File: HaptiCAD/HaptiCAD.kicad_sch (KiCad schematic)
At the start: 0 parts

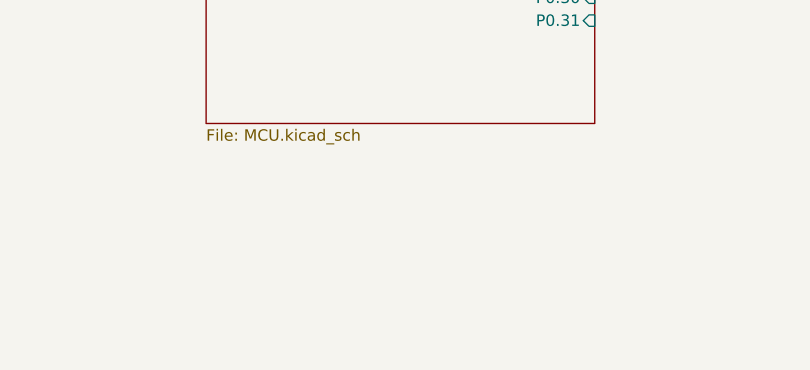
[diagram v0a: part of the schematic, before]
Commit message: Updated name, schematic and pcb
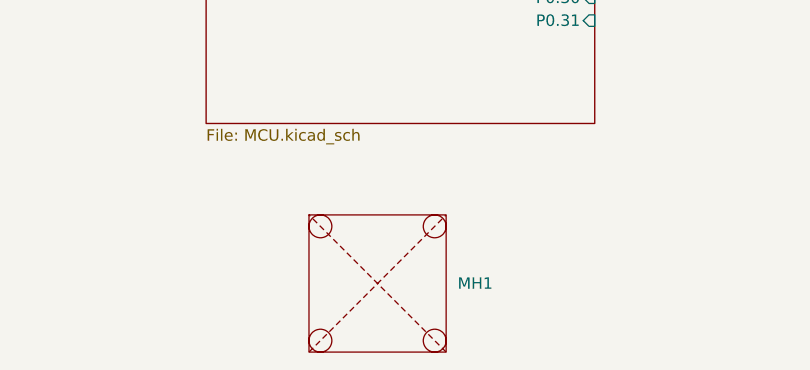
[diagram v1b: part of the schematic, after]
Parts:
- added MH1: (no value), BLDC_mount:BLDC_mount, symbol BLDC_mount:BLDC_mount
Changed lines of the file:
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@@
 (kicad_sch
-	(version 20250114)
+	(version 20260306)
 	(generator "eeschema")
-	(generator_version "9.0")
+	(generator_version "10.0")
 	(paper "A4")
 	(title_block
@@
 			(width 0)
 			(type default)
+		)
+	)
+	(symbol
+		(lib_id "BLDC_mount:BLDC_mount")
+		(at 135.89 180.34 0)
+		(unit 1)
+		(body_style 1)
+		(exclude_from_sim yes)
+		(in_bom no)
+		(on_board yes)
+		(in_pos_files yes)
+		(dnp no)
+		(fields_autoplaced yes)
+		(property "Reference" "MH1"
+			(at 144.78 180.3399 0)
+			(show_name no)
+			(do_not_autoplace no)
+			(effects
+				(font
+					(size 1.27 1.27)
+				)
+				(justify left)
+			)
+		)
+		(property "Value" ""
+			(at 135.89 180.34 0)
+			(show_name no)
+			(do_not_autoplace no)
+			(effects
+				(font
+					(size 1.27 1.27)
+				)
+			)
+		)
+		(property "Footprint" "BLDC_mount:BLDC_mount"
+			(at 135.89 180.34 0)
+			(hide yes)
+			(show_name no)
+			(do_not_autoplace no)
+			(effects
+				(font
+					(size 1.27 1.27)
+				)
+			)
+		)
+		(property "Datasheet" ""
+			(at 135.89 180.34 0)
+			(hide yes)
+			(show_name no)
+			(do_not_autoplace no)
+			(effects
+				(font
+					(size 1.27 1.27)
+				)
+			)
+		)
+		(property "Description" ""
+			(at 135.89 180.34 0)
+			(hide yes)
+			(show_name no)
+			(do_not_autoplace no)
+			(effects
+				(font
+					(size 1.27 1.27)
+				)
+			)
+		)
+		(instances
+			(project "knobber"
+				(path "/09c102b8-dfc1-4666-b1e2-d0c53b401993"
+					(reference "MH1")
+					(unit 1)
+				)
+			)
 		)
 	)
@@
 		)
 		(fill
-			(color 0 0 0 0.0000)
+			(color 0 0 0 0)
 		)
 		(property "Sheetname" "Motor driver"
 			(at 195.58 65.3284 0)
+			(show_name no)
+			(do_not_autoplace no)
 			(effects
 				(font
@@
 		(property "Sheetfile" "Motor_driver.kicad_sch"
 			(at 195.58 95.8346 0)
+			(show_name no)
+			(do_not_autoplace no)
 			(effects
 				(font
@@
 		)
 		(fill
-			(color 0 0 0 0.0000)
+			(color 0 0 0 0)
 		)
 		(property "Sheetname" "LCD"
 			(at 195.58 141.5284 0)
+			(show_name no)
+			(do_not_autoplace no)
 			(effects
 				(font
@@
 		(property "Sheetfile" "LCD.kicad_sch"
 			(at 195.58 163.1446 0)
+			(show_name no)
+			(do_not_autoplace no)
 			(effects
 				(font
@@
 		)
 		(fill
-			(color 0 0 0 0.0000)
+			(color 0 0 0 0)
 		)
 		(property "Sheetname" "LED lighting"
 			(at 195.58 51.3584 0)
+			(show_name no)
+			(do_not_autoplace no)
 			(effects
 				(font
@@
 		(property "Sheetfile" "LED_lighting.kicad_sch"
 			(at 195.58 60.2746 0)
+			(show_name no)
+			(do_not_autoplace no)
 			(effects
 				(font
@@
 		)
 		(fill
-			(color 0 0 0 0.0000)
+			(color 0 0 0 0)
 		)
 		(property "Sheetname" "Switches"
 			(at 195.58 100.8884 0)
+			(show_name no)
+			(do_not_autoplace no)
 			(effects
 				(font
@@
 		(property "Sheetfile" "Switches.kicad_sch"
 			(at 195.58 136.4746 0)
+			(show_name no)
+			(do_not_autoplace no)
 			(effects
 				(font
@@
 		)
 		(fill
-			(color 0 0 0 0.0000)
+			(color 0 0 0 0)
 		)
 		(property "Sheetname" "Sensors"
 			(at 195.58 20.8784 0)
+			(show_name no)
+			(do_not_autoplace no)
 			(effects
 				(font
@@
 		(property "Sheetfile" "Sensors.kicad_sch"
 			(at 195.58 46.3046 0)
+			(show_name no)
+			(do_not_autoplace no)
 			(effects
 				(font
@@
 		)
 		(fill
-			(color 0 0 0 0.0000)
+			(color 0 0 0 0)
 		)
 		(property "Sheetname" "Power"
 			(at 46.99 37.3884 0)
+			(show_name no)
+			(do_not_autoplace no)
 			(effects
 				(font
@@
 		(property "Sheetfile" "Power.kicad_sch"
 			(at 46.99 56.4646 0)
+			(show_name no)
+			(do_not_autoplace no)
 			(effects
 				(font
@@
 		)
 		(fill
-			(color 0 0 0 0.0000)
+			(color 0 0 0 0)
 		)
 		(property "Sheetname" "USB"
 			(at 46.99 20.8784 0)
+			(show_name no)
+			(do_not_autoplace no)
 			(effects
 				(font
@@
 		(property "Sheetfile" "USB.kicad_sch"
 			(at 46.99 32.3346 0)
+			(show_name no)
+			(do_not_autoplace no)
 			(effects
 				(font
@@
 		)
 		(fill
-			(color 0 0 0 0.0000)
+			(color 0 0 0 0)
 		)
 		(property "Sheetname" "MCU"
 			(at 116.84 20.8784 0)
+			(show_name no)
+			(do_not_autoplace no)
 			(effects
 				(font
@@
 		(property "Sheetfile" "MCU.kicad_sch"
 			(at 116.84 163.1446 0)
-			(effects
-				(font
+			(show_name no)
+			(do_not_autoplace no)
+			(effects
+				(font
